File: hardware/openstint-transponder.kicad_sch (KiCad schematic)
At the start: 38 parts, among them J1 V+, J2 V-, Q1 PMGD280UN, U1 ATtiny1616-M, U2 10 MHz, U3 SPX3819M5-L-3-3

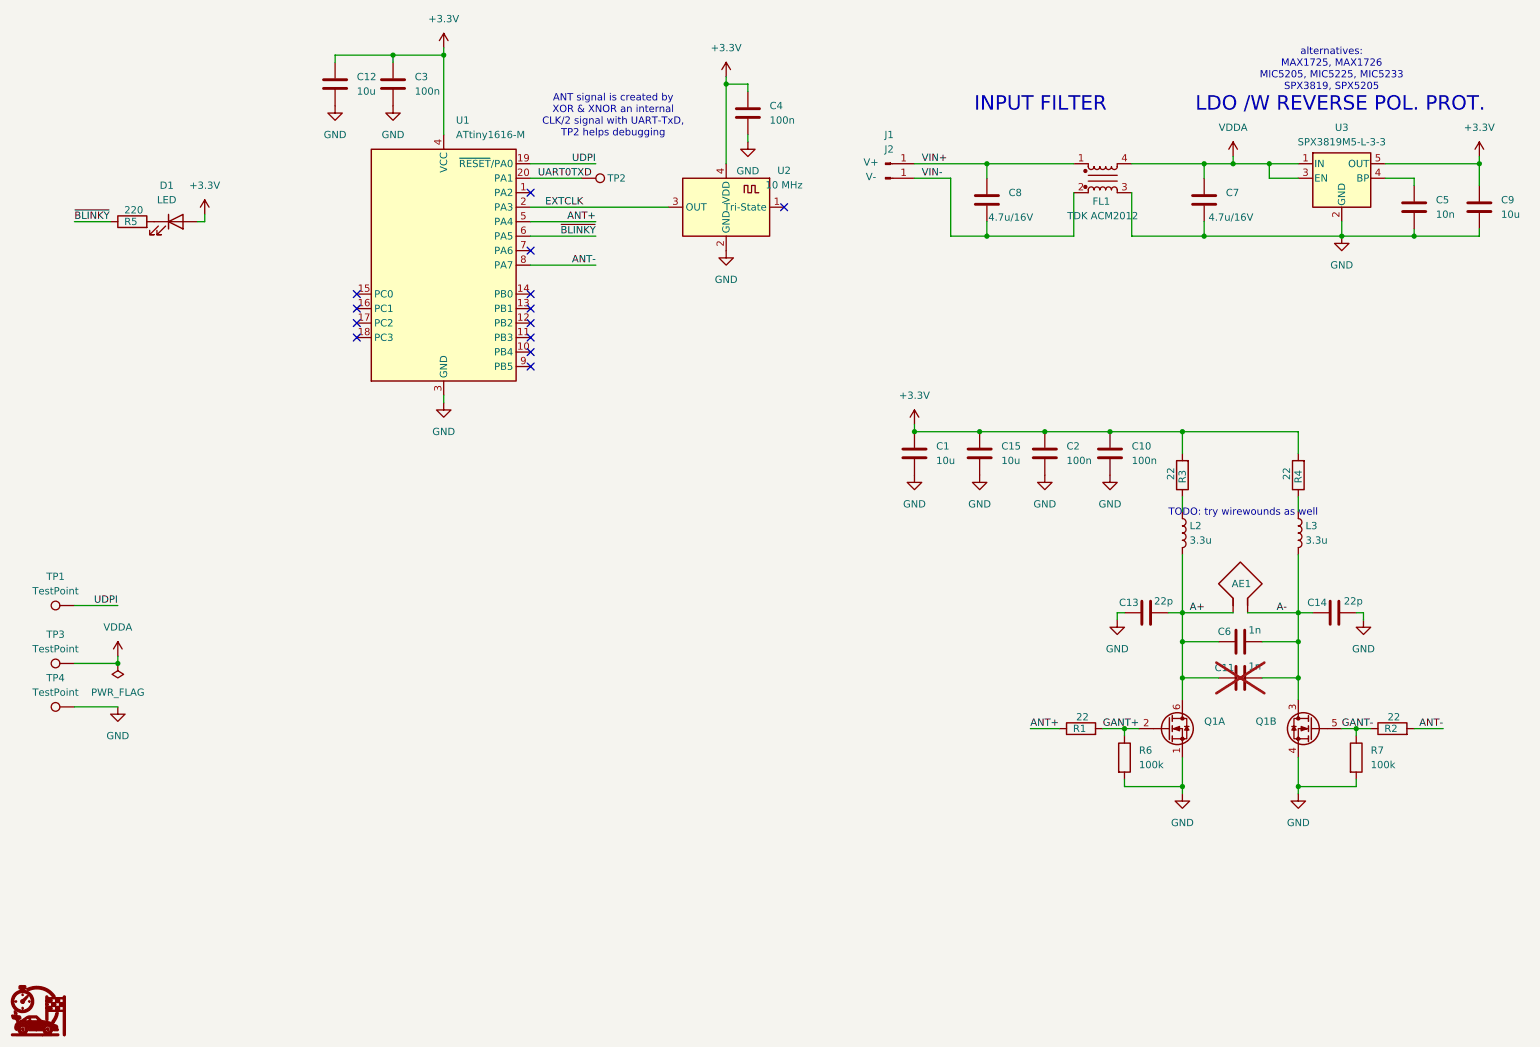
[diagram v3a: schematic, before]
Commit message: Revert "v2 transponder"
This reverts commit ef6581161f0553e0c47b9335515ce2e00a666ec4.
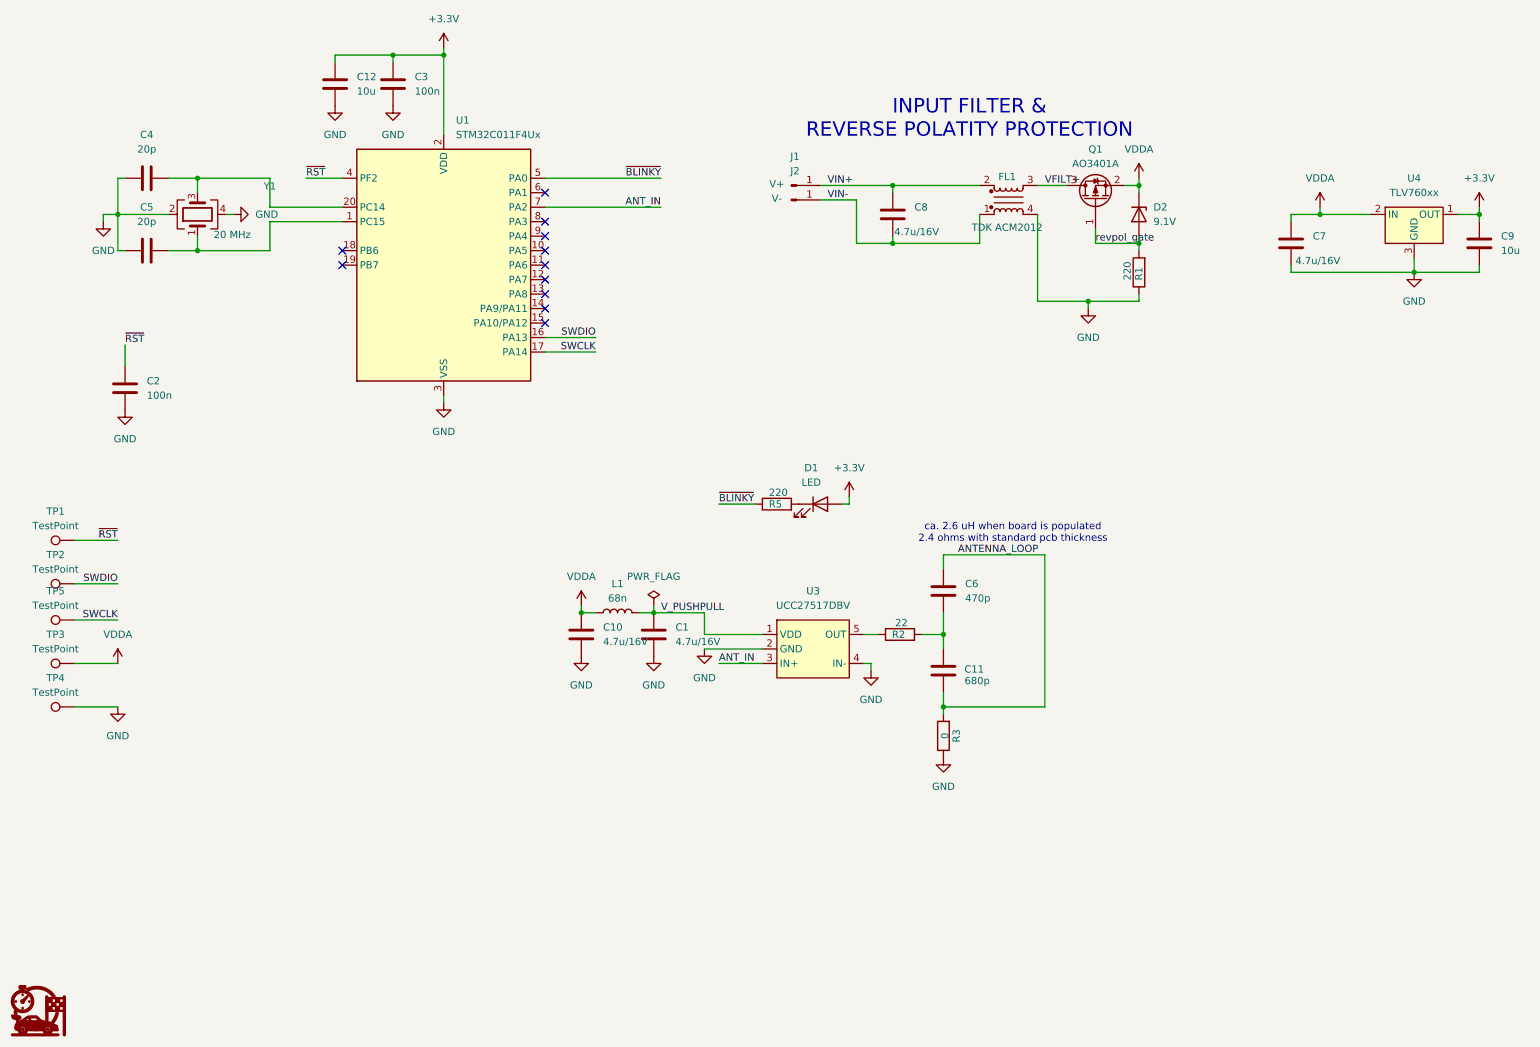
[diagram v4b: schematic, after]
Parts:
- removed AE1: Antenna_Loop, symbol Device:Antenna_Loop
- removed C13, C14: 22p, Capacitor_SMD:C_0402_1005Metric, symbol Device:C
- removed C15: 10u, Capacitor_SMD:C_0402_1005Metric, symbol Device:C
- removed L2, L3: 3.3u, Inductor_SMD:L_0603_1608Metric, symbol Device:L
- removed Q1: PMGD280UN, Package_TO_SOT_SMD:SOT-363_SC-70-6, symbol Transistor_FET:Q_Dual_NMOS_S1G1D2S2G2D1
- removed R4: 22, Resistor_SMD:R_0402_1005Metric, symbol Device:R
- removed R6, R7: 100k, Resistor_SMD:R_0402_1005Metric, symbol Device:R
- removed U1: ATtiny1616-M, Package_DFN_QFN:VQFN-20-1EP_3x3mm_P0.4mm_EP1.7x1.7mm, symbol MCU_Microchip_ATtiny:ATtiny1616-M
- removed U2: 10 MHz, Crystal:Crystal_SMD_3225-4Pin_3.2x2.5mm, symbol symbols:Oscillator
- removed U3: SPX3819M5-L-3-3, Package_TO_SOT_SMD:SOT-23-5, symbol Regulator_Linear:SPX3819M5-L-3-3
- added D2: 9.1V, Diode_SMD:D_SOD-323, symbol Device:D_Zener
- added L1: 68n, Inductor_SMD:L_0603_1608Metric, symbol Device:L
- added Q1: AO3401A, Package_TO_SOT_SMD:SOT-23, symbol Transistor_FET:AO3401A
- added TP5: TestPoint, TestPoint:TestPoint_Pad_D1.0mm, symbol Connector:TestPoint
- added U1: STM32C011F4Ux, Package_DFN_QFN:ST_UFQFPN-20_3x3mm_P0.5mm, symbol MCU_ST_STM32C0:STM32C011F4Ux
- added U3: UCC27517DBV, Package_TO_SOT_SMD:SOT-23-5, symbol Driver_FET:UCC27517DBV
- added U4: TLV760xx, Package_TO_SOT_SMD:SOT-23, symbol Regulator_Linear:TLV760xx
- added Y1: 20 MHz, Crystal:Crystal_SMD_3225-4Pin_3.2x2.5mm, symbol Device:Crystal_GND24
- C1: value 10u -> 4.7u/16V; footprint Capacitor_SMD:C_0402_1005Metric -> Capacitor_SMD:C_0603_1608Metric; LCSC C15525 -> C19666
- C10: value 100n -> 4.7u/16V; footprint Capacitor_SMD:C_0402_1005Metric -> Capacitor_SMD:C_0603_1608Metric; LCSC C1525 -> C19666
- C11: value 1n -> 680p; footprint Capacitor_SMD:C_0402_1005Metric -> Capacitor_SMD:C_0603_1608Metric; LCSC C1523 -> C30816; now fitted
- C4: value 100n -> 20p; LCSC C1525 -> C1554
- C5: value 10n -> 20p; LCSC C15195 -> C1554
- C6: value 1n -> 470p; footprint Capacitor_SMD:C_0402_1005Metric -> Capacitor_SMD:C_0603_1608Metric; LCSC C1523 -> C1620
- R1: value 22 -> 220; LCSC C25092 -> C25091
- R3: value 22 -> 0; LCSC C25092 -> C17168
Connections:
- net ANT+ is gone; now on net GND: R1.1
- net ANT- is gone; now on an unnamed net: R2.2
- net +3.3V: now also U1.2 (VDD), U4.1 (OUT); no longer C1.1, C10.2, C2.2, C4.2, R3.2
- net GND: now also C10.2, C2.2, C5.1, FL1.4, R3.1, U1.3 (VSS), U3.2 (GND), U3.4 (IN-), U4.3 (GND), Y1.2, Y1.4; no longer C10.1, C2.1, C5.2, FL1.3
- net VDDA: now also C10.1, D2.1 (K), L1.1, Q1.2 (S), U4.2 (IN); no longer FL1.4
- net VIN+: now also FL1.2; no longer FL1.1
- net VIN-: now also FL1.1; no longer FL1.2
- net ~{BLINKY}: now also U1.5 (PA0)
- net A+: no longer names the net of C11.1
- net A+: now also C6.2; no longer C6.1
- net A- renamed ANTENNA_LOOP
- net ANTENNA_LOOP: now also C6.1, R3.2; no longer C6.2
- net GANT+ renamed revpol_gate
- net revpol_gate: now also D2.2 (A), Q1.1 (G)
- net GANT-: no longer names the net of R2.1
- net GANT-: now also U3.5 (OUT)
- net UART0TXD renamed SWDIO
- net SWDIO: now also U1.16 (PA13)
- net UDPI renamed ~{RST}
- net ~{RST}: now also C2.1, U1.4 (PF2)
- new net: C5.2, U1.1 (PC15), Y1.1
- new net: C4.2, U1.20 (PC14), Y1.3
- new net ANT_IN: U1.7 (PA2), U3.3 (IN+)
- new net SWCLK: TP5.1, U1.17 (PA14)
- new net VFILT+: FL1.3, Q1.3 (D)
- new net V_PUSHPULL: C1.1, L1.2, U3.1 (VDD)
- no-connect marks 13 -> 11
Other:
- note added: "INPUT FILTER & REVERSE POLATITY PROTECTION"
- note added: "ca. 2.6 uH when board is populated 2.4 ohms with standard pcb thickness"
- note removed: "ANT signal is created by XOR & XNOR an internal CLK/2 signal with UART-TxD, TP2 helps debugging"
- note removed: "INPUT FILTER"
- note removed: "LDO /W REVERSE POL. PROT."
- note removed: "TODO: try wirewounds as well"
- note removed: "alternatives: MAX1725, MAX1726 MIC5205, MIC5225, MIC5233 SPX3819, SPX5205"
- moved on the sheet: C7, C8, C9, D1, FL1, J1, J2, R5, TP1
